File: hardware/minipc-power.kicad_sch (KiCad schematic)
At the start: 104 parts, among them J1 USB-C (HRO TYPE-C-31-M-12), J10 VSYS (to switch), J11 CHG, J12 PG_CHG, J13 VBAT_SENSE, J14 3V3_PG, J15 GND, J16 GND, J17 GND, J2 BAT+, J3 BAT-, J4 NTC, J5 NTC-, J6 +12V OUT, J7 +5V OUT, J8 +3V3 OUT, J9 EN (to switch), Q1 CSD13202Q2, Q2 CSD13202Q2, Q3 CSD13202Q2, Q4 CSD25404Q3, Q5 CSD25404Q3, Q6 2N7002, U1 CH224Q, U2 BQ25606, U3 HY2113-MB1A, U4 TPS61178, U5 TPS61088-Q1, U6 TPS63802

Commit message: Schematic refinement pass: spacing, field placement, symbol rows, 3V3 block moved; skill-gap notes on an s-expression layer
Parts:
- C10, C17, C18, C19, C34, C9: value 22uF 25V -> 22uF; Voltage (none) -> 25V
- C12, C7: value 4.7uF 16V -> 4.7uF; Voltage (none) -> 16V
- C14, C15: value 4.7uF 25V -> 4.7uF; Voltage (none) -> 25V
- C20, C21, C22, C3, C5: value 10uF 25V -> 10uF; Voltage (none) -> 25V
- C30, C31: value 47uF 16V -> 47uF; Voltage (none) -> 16V
- C33: value 22uF 6.3V -> 22uF; Voltage (none) -> 6.3V
- C6: value 10uF 10V -> 10uF; Voltage (none) -> 10V
- F1: value 10A 0451010 -> 10A
- J1: value USB-C (HRO TYPE-C-31-M-12) -> USB-C HRO TYPE-C-31-M-12
- J10: value VSYS (to switch) -> VSYS (switch)
- J9: value EN (to switch) -> EN (switch)
- L1: value 2.2uH FXL0630-2R2-M -> 2.2uH
- L2: value 3.3uH FXL0630-3R3-M -> 3.3uH
- L3: value 1uH FXL0630-1R0-M -> 1uH
- L4: value 0.47uH FXL0530-R47-M -> 0.47uH
- LED1: value red (charging) -> red
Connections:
- net +3V3: now also R26.2; no longer R26.1
- net 3V3_PG: now also R26.1; no longer R26.2
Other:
- note added: "1S2P pack: fuse, reverse block, HY2113 protector"
- note added: "2.96 V at 4.35 V, 3 uA"
- note added: "Charger BQ25606: standalone NVDC, 1.44 A charge, 1.92 A input limit"
- note added: "FB senses after Q4 (VOUT2), as in datasheet fig. 22. Rgate/Cgate: Vgs = 178k x 55 uA = 9.8 V, ~0.5 ms turn-on."
- note added: "ILIM 249R -> 1.92 A (<= 2 A of an 18 W PD charger) ICHG 470R -> 1.44 A VSET open -> 4.208 V"
- note added: "ILIM = 550000 / 69.8k = 7.9 A (-Q1 has a 0.6 V ILIM reference) FSW 267k (to SW) = 594 kHz, SS 10 nF = 2.4 ms"
- note added: "Q1: a reversed pack turns it off and its body diode blocks, so U3 never sees reverse voltage. Trip: 250 mV / (Q2+Q3) = ~8 A hot ... ~15 A cold."
- note added: "R1 6.8k selects 9 V (CH224 table 5-1). Charger D+/D- are left open on purpose: ILIM sets the input limit."
- note added: "RT1 5.23k / RT2 30.9k: 0-60 C window with a 103AT NTC from J4 to J5 (GND)"
- note added: "Switch closed = on: U4, U5, U6 run and Q6 closes the 5 V switch. Charging works with the switch open."
- note removed: "1S2P pack: reverse block, HY2113 protector, fuse"
- note removed: "2.96 V at 4.35 V; 3 uA"
- note removed: "Charger BQ25606 (standalone NVDC, 1.44 A charge, 1.92 A input limit)"
- note removed: "FB senses after Q4 (VOUT2)"
- note removed: "NTC 10k B3435 (103AT) from J4 to J5 (GND), taped to the pack"
- note removed: "R1 6.8k = 9 V request (CH224 table 5-1)"
- note removed: "Reversed pack: Q1 off, body diode blocks, U3 never sees reverse voltage"
- note removed: "Switch closed = on. EN high: U4, U5, U6 run and Q6 closes the 5 V switch."

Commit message: Board stage 1: 4-layer JLC04161H-7628 board from the schematic netlist (parity clean), rules, net classes, courtyards on imported footprints
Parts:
- H1, H2, J10, J11, J12, J13, J14, J15, J16, J17, J2, J3, J4, J5, J6, J7, J8, J9: now left out of the parts list

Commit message: Pad labels on both silkscreens, round GND/negative pads, refs moved to fab layer, 3D models for F1 and J1
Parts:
- J15, J16, J17, J3: footprint TestPoint:TestPoint_THTPad_2.5x2.5mm_Drill1.2mm -> TestPoint:TestPoint_THTPad_D2.5mm_Drill1.2mm
- J5: footprint TestPoint:TestPoint_THTPad_2.0x2.0mm_Drill1.0mm -> TestPoint:TestPoint_THTPad_D2.0mm_Drill1.0mm

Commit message: Drop CH224Q D+/D- (PD uses CC), re-orient U1, charger-area placement for routability; routing infrastructure
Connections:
- now unconnected: J1.A6 (D+), J1.A7 (D-), J1.B6 (D+), J1.B7 (D-), U1.4 (DP), U1.5 (DM)
- no-connect marks 13 -> 19
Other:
- note added: "R1 6.8k selects 9 V (CH224 table 5-1). D+/D- open on purpose (PD uses CC; charger ILIM sets the input limit only with D+/D- open)."
- note removed: "R1 6.8k selects 9 V (CH224 table 5-1). Charger D+/D- are left open on purpose: ILIM sets the input limit."

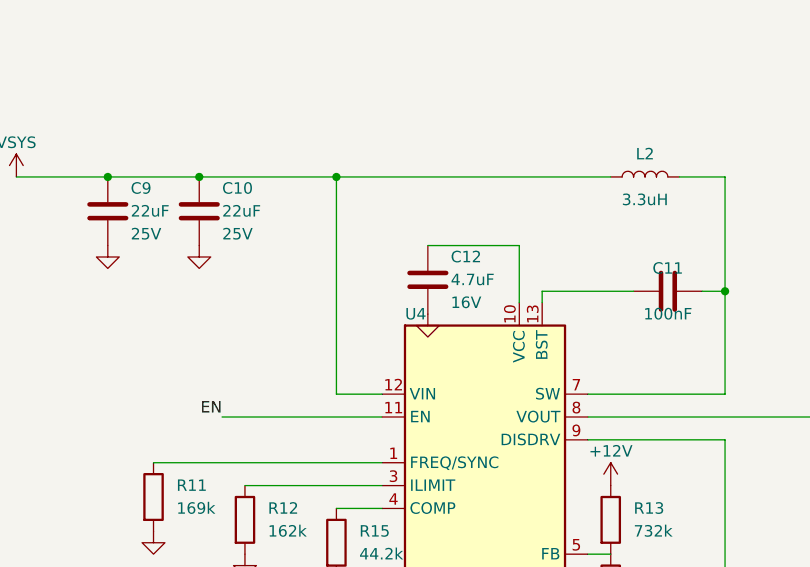
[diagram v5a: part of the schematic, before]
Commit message: Add C37 1uF 0402 VIN-pin bypass for the 12V boost (TPS61178 layout rule 5); board regeneration pending (KiCad open)
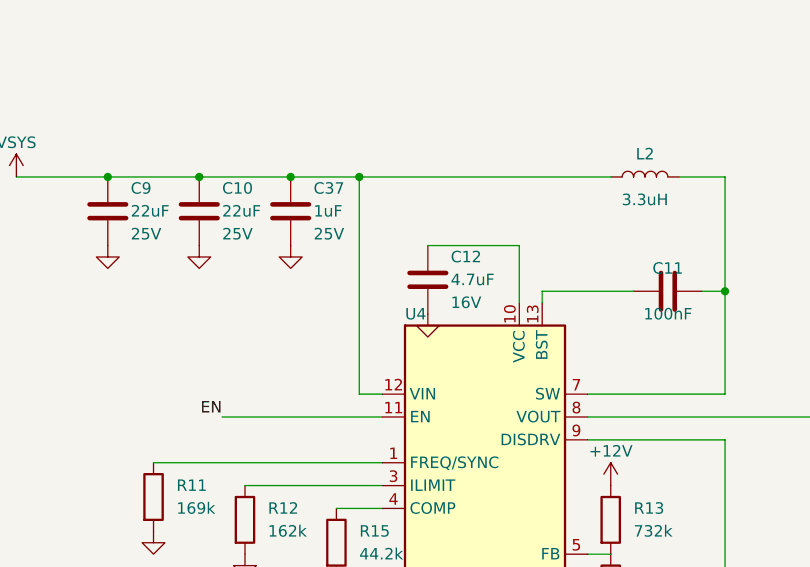
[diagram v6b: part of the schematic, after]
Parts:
- added C37: 1uF, Capacitor_SMD:C_0402_1005Metric, symbol Device:C
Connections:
- net GND: now also C37.2
- net VSYS: now also C37.1

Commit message: Design review 2026-10-24 (kicad-skills board review): fixes, datasheet links on every part
Fixes found by the review (docs/review-2026-10-24.md):
- R25 91k: LCSC C4147 (2 in stock) -> C144733
- U5 TPS61088-Q1: C38 1 uF 0402 at the VOUT pins (datasheet fig. 13 C9, fig. 21); NC pins 11/12 tied to GND
  as the pin table asks (symbol pins passive)
- Q5 load switch: C32 10 nF -> 100 nF (~1 ms turn-on; inrush could trip the BQ25606 BATFET OCP latch)
- U6 TPS63802: C33 ground on a top-layer track to PGND pin 8 (fig. 12-1); C_OUT side still open
- R7 330 -> 100 R (HY2113 100-200 R); R16 178k -> 100k (Q4 Vgs margin to +/-12 V)
- power-design.md / layout-compliance.md corrected against the board (R_ICHG, L4, SS, COUT1, Q2/Q3 common drain)

Datasheet links: every BOM part carries one in the schematic and on the board (TI symlinks for TI parts, else the
LCSC page of the exact part). The redrawn symbols had dropped JLCImport's links, passives kept KiCad's "~" and
board_setup never copied the netlist's datasheet; schgen, symbols.library() and board_setup now refuse a BOM part
without one. kicad-skills partfields.py --online: 0 problems (176 before).

Pin decisions for U2.2 and U3.4 (NC per their pin tables), required by kicad-skills' stricter nc_audit.
KiCad's own project / fab-toolkit files and the production outputs (gerbers, BOM, positions) included.
skill-gaps.md: gaps 34-45 from running the review skills.
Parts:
- added C38: 1uF, Capacitor_SMD:C_0402_1005Metric, symbol Device:C
- C32: value 10nF -> 100nF; LCSC C15195 -> C1525
- R16: value 178k -> 100k; LCSC C26995 -> C25741
- R25: LCSC C4147 -> C144733
- R7: value 330 -> 100; LCSC C25104 -> C25076
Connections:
- net GND: now also U5.11 (NC), U5.12 (NC), C38.2
- net at C30.1, C31.1, C32.1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: now also C38.1
- no-connect marks 19 -> 17
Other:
- moved on the sheet: C30, C31, C32, J7, Q5, Q6, R22, R23
